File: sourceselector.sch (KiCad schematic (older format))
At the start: 42 parts, among them J14 RCAJack, J15 RCAJack, J16 XLR4BODYPIN, J17 XLR4BODYPIN, J18 RCAJack, J19 RCAJack, J20 RCAJack, J21 RCAJack, J22 Jack-DC, J23 Conn_01x02, J24 Conn_01x02, SW2 SW_SPST, SW3 SW_SPST, U10 THAT1200, U11 THAT1200

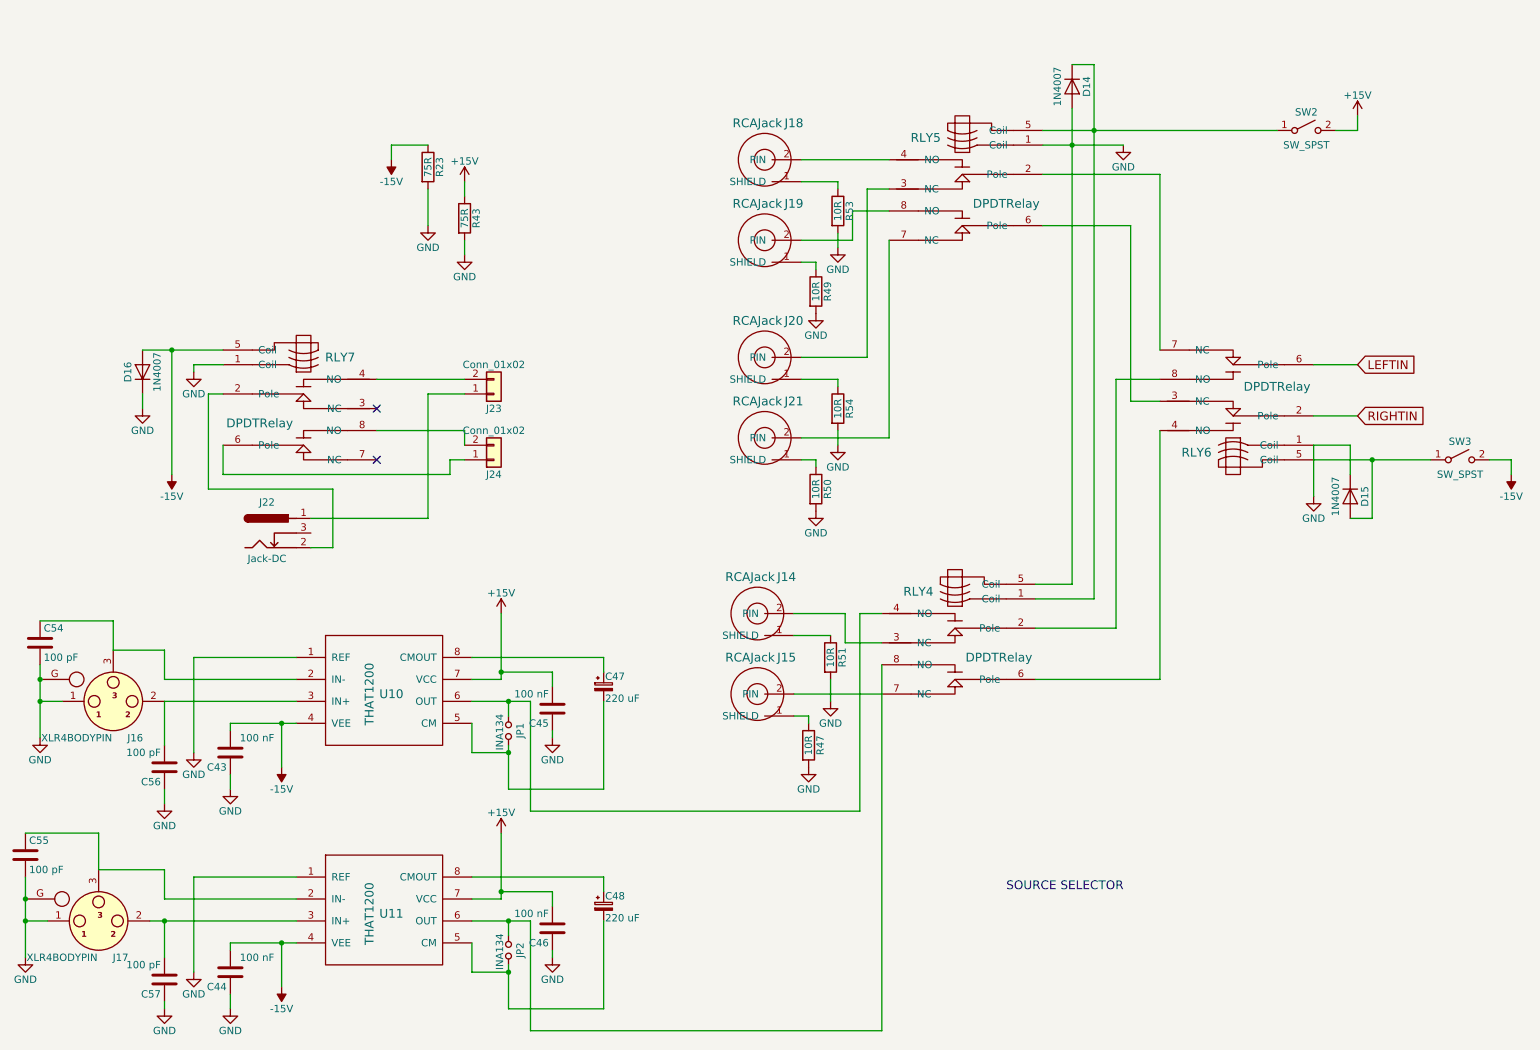
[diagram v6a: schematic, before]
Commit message: remove screwy UVLO
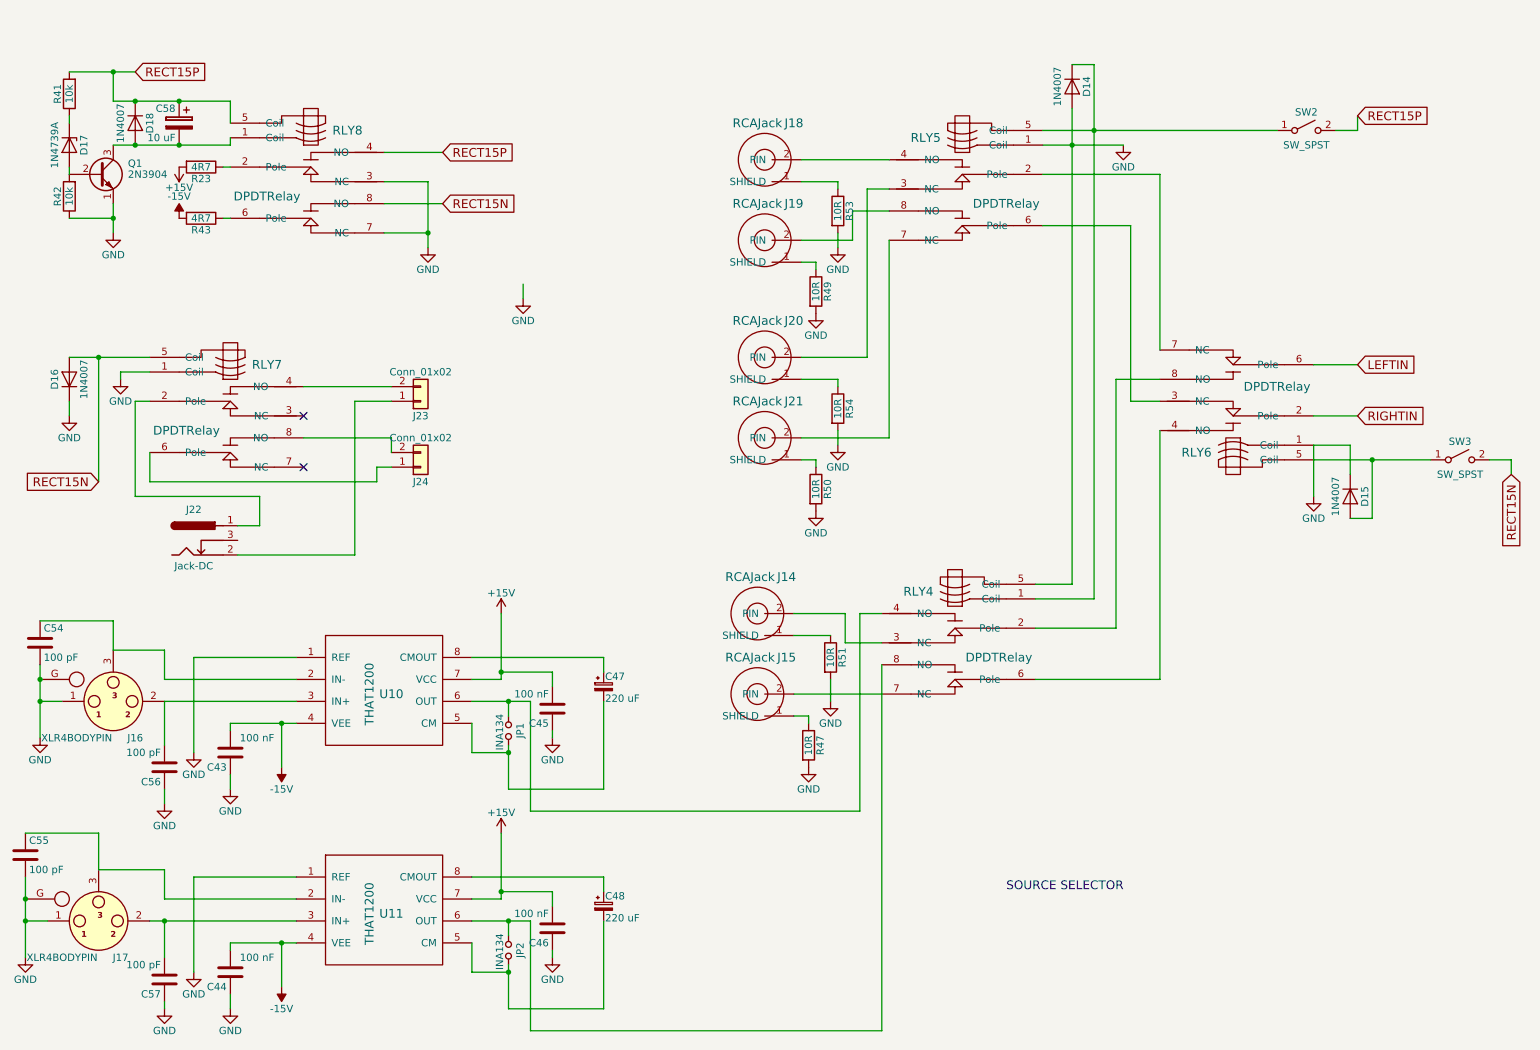
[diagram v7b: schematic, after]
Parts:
- added C58: 10 uF, Capacitors_THT:CP_Radial_D5.0mm_P2.50mm, symbol CP
- added D17: 1N4739A, Diodes_THT:D_DO-41_SOD81_P7.62mm_Horizontal, symbol D_Zener
- added D18: 1N4007, Diodes_THT:D_DO-41_SOD81_P7.62mm_Horizontal, symbol D
- added Q1: 2N3904, TO_SOT_Packages_THT:TO-92_Inline_Wide, symbol 2N3904
- added R41, R42: 10k, Resistors_THT:R_Axial_DIN0207_L6.3mm_D2.5mm_P7.62mm_Horizontal, symbol R
- added RLY8: DPDTRelay, Preamp:G2VRelay, symbol DPDTRelay
- R23, R43: value 75R -> 4R7
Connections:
- net +15V: now also R23.2; no longer R43.1, SW2.2 (B)
- net -15V: now also R43.2; no longer D16.2 (A), R23.1, RLY7.5 (Coil), SW3.2 (B)
- net GND: now also Q1.1 (E), R42.1, RLY8.3 (NC), RLY8.7 (NC); no longer R23.2, R43.2
- net at RLY7.2 (Pole): now also J22.1; no longer J22.2
- net at J23.1 (Pin_1): now also J22.2; no longer J22.1
- new net: C58.2, D18.2 (A), Q1.3 (C), RLY8.1 (Coil)
- new net: R23.1, RLY8.2 (Pole)
- new net: R43.1, RLY8.6 (Pole)
- new net: D17.2 (A), Q1.2 (B), R42.2
- new net: D17.1 (K), R41.1
- new net RECT15N: D16.2 (A), RLY7.5 (Coil), RLY8.8 (NO), SW3.2 (B)
- new net RECT15P: C58.1, D18.1 (K), R41.2, RLY8.4 (NO), RLY8.5 (Coil), SW2.2 (B)
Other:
- moved on the sheet: D16, J22, J23, J24, R23, R43, RLY7

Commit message: Now grounds all of the outputs when supply is below 20 V
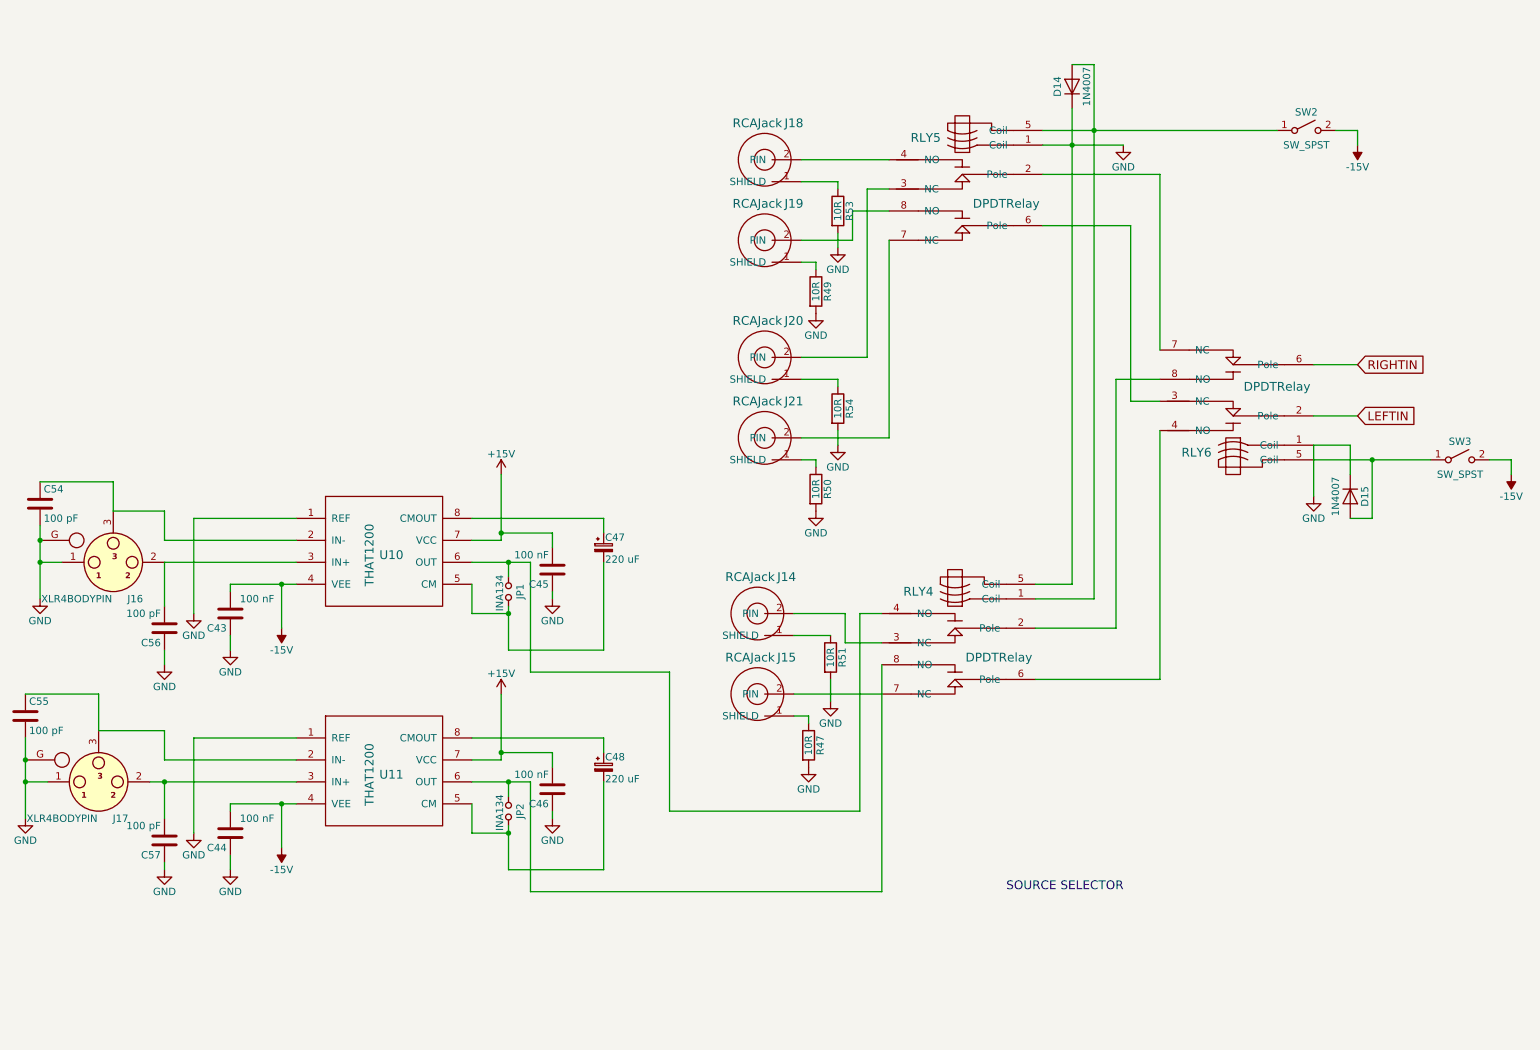
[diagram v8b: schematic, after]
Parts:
- removed C58: 10 uF, Capacitors_THT:CP_Radial_D5.0mm_P2.50mm, symbol CP
- removed D16, D18: 1N4007, Diodes_THT:D_DO-41_SOD81_P7.62mm_Horizontal, symbol D
- removed D17: 1N4739A, Diodes_THT:D_DO-41_SOD81_P7.62mm_Horizontal, symbol D_Zener
- removed J22: Jack-DC, Connectors:BARREL_JACK, symbol Jack-DC
- removed J23, J24: Conn_01x02, Connectors_Terminal_Blocks:TerminalBlock_bornier-2_P5.08mm, symbol Conn_01x02
- removed Q1: 2N3904, TO_SOT_Packages_THT:TO-92_Inline_Wide, symbol 2N3904
- removed R23, R43: 4R7, Resistors_THT:R_Axial_DIN0309_L9.0mm_D3.2mm_P12.70mm_Horizontal, symbol R
- removed R41, R42: 10k, Resistors_THT:R_Axial_DIN0207_L6.3mm_D2.5mm_P7.62mm_Horizontal, symbol R
- removed RLY7, RLY8: DPDTRelay, Preamp:G2VRelay, symbol DPDTRelay
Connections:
- net RECT15N is gone; now on net -15V: SW3.2 (B)
- net RECT15P is gone; now on net -15V: SW2.2 (B)
- net GND: now also D14.1 (K); no longer D14.2 (A)
- net LEFTIN: now also RLY6.2 (Pole); no longer RLY6.6 (Pole)
- net RIGHTIN: now also RLY6.6 (Pole); no longer RLY6.2 (Pole)
- net at RLY4.1 (Coil), RLY5.5 (Coil), SW2.1 (A): now also D14.2 (A); no longer D14.1 (K)
- no-connect marks 2 -> 0
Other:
- moved on the sheet: C43, C44, C45, C46, C47, C48, C54, C55, C56, C57, J16, J17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
